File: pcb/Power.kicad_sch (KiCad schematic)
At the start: 20 parts, among them J12 JST_2mm_LiPo, J13 Screw_Terminal_01x02, U1 TPS63020DSJR, U2 CN3170

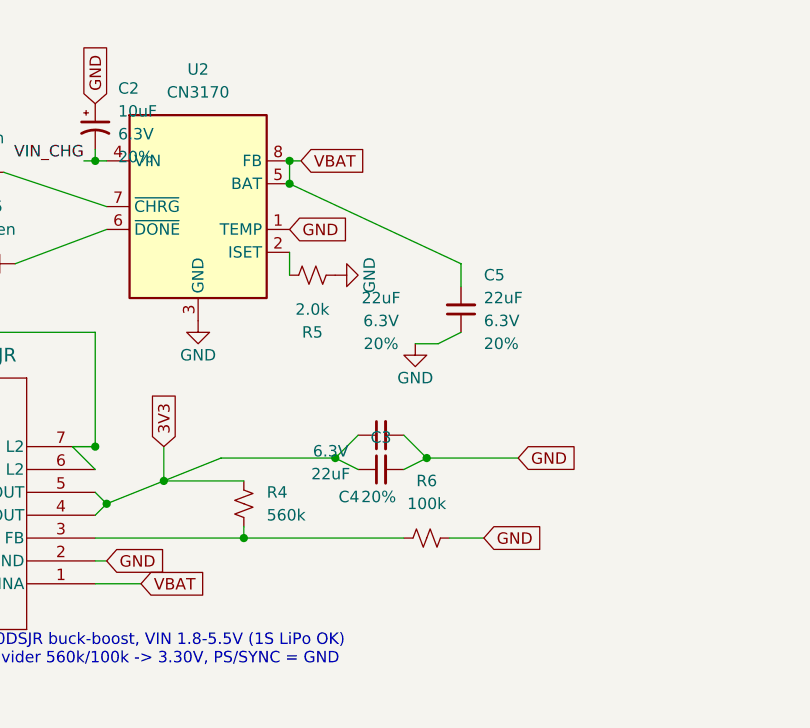
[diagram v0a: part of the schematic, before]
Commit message: adds a resistor between TMP and GND in Power sheet to allow battery charging
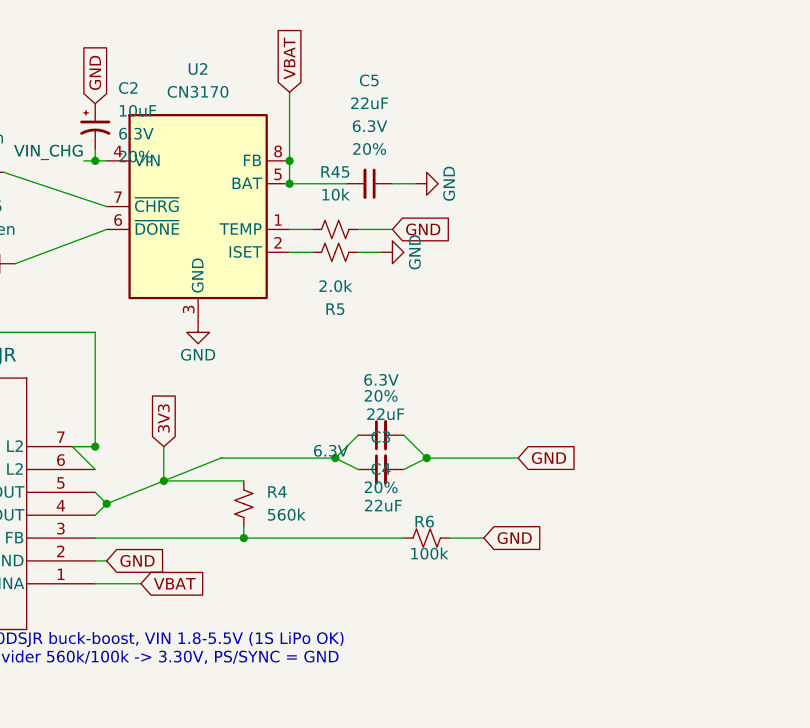
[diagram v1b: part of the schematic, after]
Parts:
- added R45: 10k, PCM_SparkFun-Resistor:R_0603_1608Metric, symbol PCM_SparkFun-Resistor:10k_0603
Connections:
- net GND: now also R45.2; no longer U2.1 (TEMP)
- new net: R45.1, U2.1 (TEMP)
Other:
- moved on the sheet: C5, R5
